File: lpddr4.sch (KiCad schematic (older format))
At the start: 43 parts, among them U1 MT53E256M16D1

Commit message: Remove note
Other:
- note removed: "TODO: connect to FPGA IO"
- note removed: "TODO\nAdd reset handling\nADD ODT/ZQ control"
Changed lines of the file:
@@
 Text GLabel 10900 2300 1    50   Input ~ 0
 VDD2
-Text Notes 7350 6050 0    98   ~ 20
-TODO\nAdd reset handling\nADD ODT/ZQ control
 Text GLabel 9350 3050 0    50   Input ~ 0
 CS0_B
@@
 Wire Wire Line
 	6175 2850 6375 2850
-Text Notes 13075 2025 0    98   ~ 20
-TODO: connect to FPGA IO
 $Comp
 L antmicroCapacitorsmisc:C_100n_0201 C1

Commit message: Add OSHW logotype
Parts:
- added N?: oshw_logo, antmicro-footprints:oshw-logo, symbol antmicroMechanicalParts:oshw_logo
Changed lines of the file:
@@
 Wire Wire Line
 	12050 3450 12050 3525
+$Comp
+L antmicroMechanicalParts:oshw_logo N?
+U 1 1 6001ECE6
+P 11900 9575
+F 0 "N?" H 12094 9578 50  0000 L CNN
+F 1 "oshw_logo" H 12094 9487 50  0000 L CNN
+F 2 "antmicro-footprints:oshw-logo" H 11920 9335 50  0001 C CNN
+F 3 "" H 11900 9575 50  0001 C CNN
+	1    11900 9575
+	1    0    0    -1
+$EndComp
 $EndSCHEMATC

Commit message: Optimize pairs of buried vias
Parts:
- gave numbers to parts that had none: 1
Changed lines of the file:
@@
 Title ""
 Date ""
-Rev ""
+Rev "1.0.0"
 Comp ""
 Comment1 ""
@@
 	12050 3450 12050 3525
 $Comp
-L antmicroMechanicalParts:oshw_logo N?
+L antmicroMechanicalParts:oshw_logo N3
 U 1 1 6001ECE6
 P 11900 9575
-F 0 "N?" H 12094 9578 50  0000 L CNN
+F 0 "N3" H 12094 9578 50  0000 L CNN
 F 1 "oshw_logo" H 12094 9487 50  0000 L CNN
 F 2 "antmicro-footprints:oshw-logo" H 11920 9335 50  0001 C CNN

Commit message: Update local libs, resolve DRC
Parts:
- C1, C10, C11, C12, C13, C14, C15, C16, C17, C18, C19, C2, C20, C21, C22, C23, C24, C25, C26, C27, C28, C29, C3, C30, C31, C32, C33, C35, C36, C4, C5, C6, C7, C8, C9: footprint antmicro-footprints:0201-res -> lpddr4-testbed-footprints:0201-res; symbol antmicroCapacitorsmisc:C_100n_0201 -> lpddr4-testbed:C_100n_0201
- N3: footprint antmicro-footprints:oshw-logo -> lpddr4-testbed-footprints:oshw-logo; symbol antmicroMechanicalParts:oshw_logo -> lpddr4-testbed:oshw_logo
- R1, R3, R4, R5: footprint antmicro-footprints:0402-res -> lpddr4-testbed-footprints:0402-res; symbol antmicroResistors0402:R_10k_0402 -> lpddr4-testbed:R_10k_0402
- R2, R7: footprint antmicro-footprints:0402-res -> lpddr4-testbed-footprints:0402-res; symbol antmicroResistors0402:R_0R_0402 -> lpddr4-testbed:R_0R_0402
- R6: footprint antmicro-footprints:0402-res -> lpddr4-testbed-footprints:0402-res; symbol antmicroResistors0402:R_240R_0402 -> lpddr4-testbed:R_240R_0402

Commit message: Update DRAM MPN
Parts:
- U1: value MT53E256M16D1 -> MT53E256M32D2DS-053; symbol lpddr4-testbed:MT53E256M16D1 -> lpddr4-testbed:MT53E256M32D2DS-053; MPN (none) -> MT53E256M32D2DS-053 WT:B; Manufacturer (none) -> Micron
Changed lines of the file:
@@
 LPDDR4
 $Comp
-L lpddr4-testbed:MT53E256M16D1 U1
+L lpddr4-testbed:MT53E256M32D2DS-053 U1
 U 1 1 602BB4A5
 P 4650 4050
-F 0 "U1" H 4125 5425 50  0000 C CNN
-F 1 "MT53E256M16D1" H 4200 2675 50  0000 C CNN
+F 0 "U1" H 4900 2675 50  0000 C CNN
+F 1 "MT53E256M32D2DS-053" H 4200 2675 50  0001 C CNN
 F 2 "lpddr4-testbed-footprints:BGA-200_10.0x14.5mm_Layout12x22_P0.80x0.65mm" H 4700 2150 50  0001 C CNN
 F 3 "" H 4550 2850 50  0001 C CNN
+F 4 "MT53E256M32D2DS-053 WT:B" H 5400 2525 50  0000 C CNN "MPN"
+F 5 "Micron" H 4950 2600 50  0000 C CNN "Manufacturer"
 	1    4650 4050
 	1    0    0    -1
@@
 	12375 2950 12375 2725
 $Comp
-L lpddr4-testbed:MT53E256M16D1 U1
+L lpddr4-testbed:MT53E256M32D2DS-053 U1
 U 2 1 602BF408
 P 10900 4050
-F 0 "U1" H 10350 5425 50  0000 C CNN
-F 1 "MT53E256M16D1" H 10450 2675 50  0000 C CNN
+F 0 "U1" H 11150 2700 50  0000 C CNN
+F 1 "MT53E256M32D2DS-053" H 10450 2675 50  0001 C CNN
 F 2 "lpddr4-testbed-footprints:BGA-200_10.0x14.5mm_Layout12x22_P0.80x0.65mm" H 10950 2150 50  0001 C CNN
 F 3 "" H 10800 2850 50  0001 C CNN
+F 4 "MT53E256M32D2DS-053 WT:B" H 11650 2550 50  0000 C CNN "MPN"
+F 5 "Micron" H 11200 2625 50  0000 C CNN "Manufacturer"
 	2    10900 4050
 	1    0    0    -1

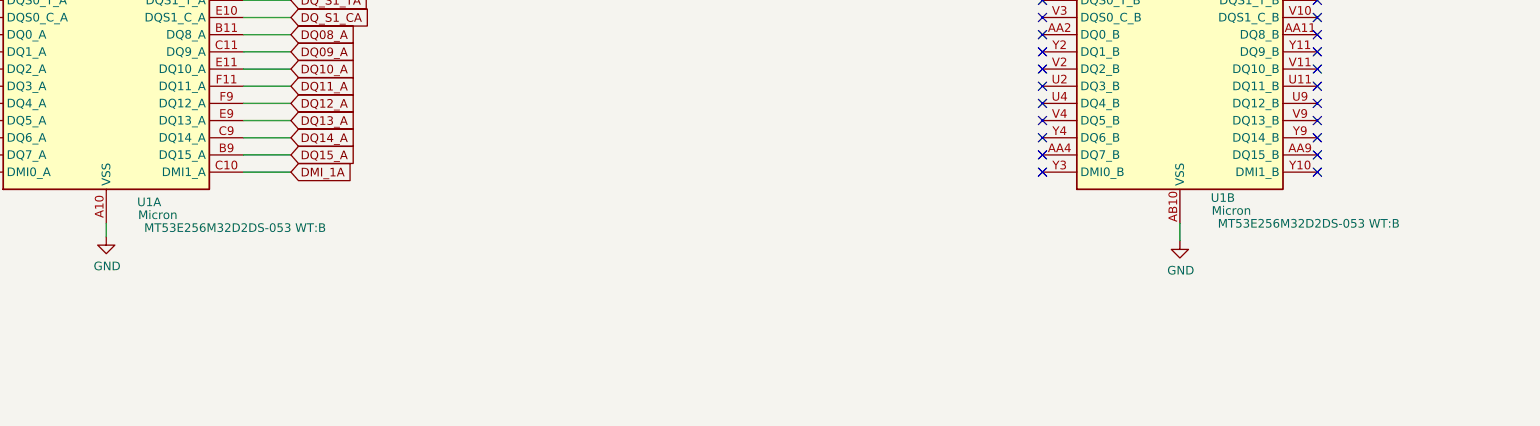
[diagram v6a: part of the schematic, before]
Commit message: Changed DDR type to MT53E1G32D2NP-046 WT:A
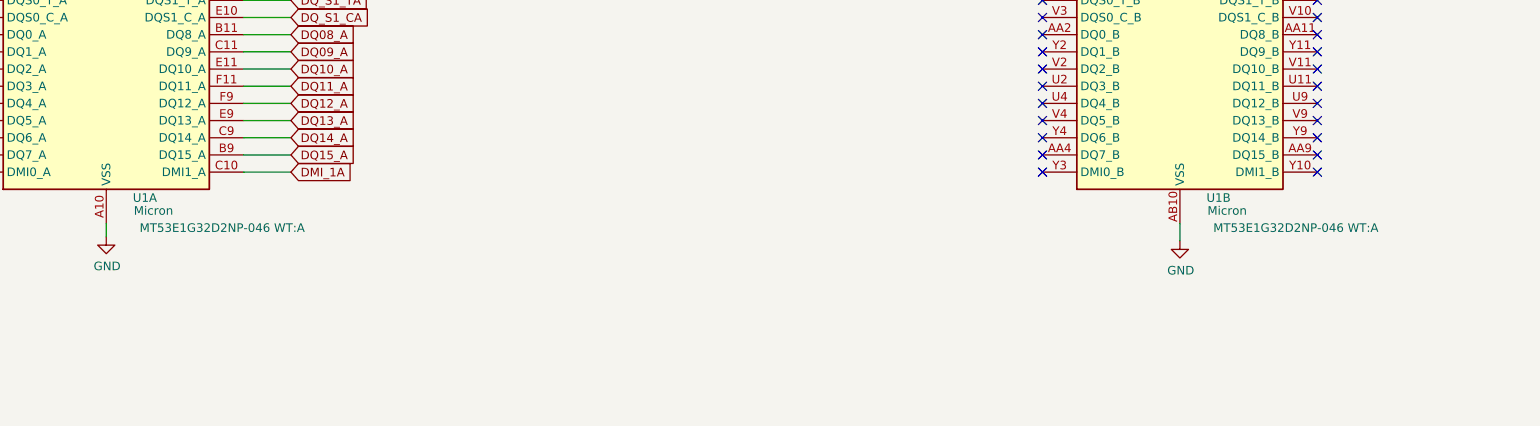
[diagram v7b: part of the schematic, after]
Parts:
- removed U1: MT53E256M32D2DS-053, lpddr4-testbed-footprints:BGA-200_10.0x14.5mm_Layout12x22_P0.80x0.65mm, symbol lpddr4-testbed:MT53E256M32D2DS-053
- added U1: MT53E1G32D2NP-046, lpddr4-testbed-footprints:BGA-200_10.0x14.5mm_Layout12x22_P0.80x0.65mm, symbol lpddr4-testbed:MT53E1G32D2NP-046
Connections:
- net CA2_A: now also U1.H9 (CA2_A)
- net CA3_A: now also U1.H10 (CA3_A)
- net CA4_A: now also U1.H11 (CA4_A)
- net CA5_A: now also U1.J11 (CA5_A)
- net CA_0A: now also U1.H2 (CA0_A)
- net CA_1A: now also U1.J2 (CA1_A)
- net CKE0_A: now also U1.J4 (CKE0_A)
- net CK_CA: now also U1.J9 (CK_C_A)
- net CK_TA: now also U1.J8 (CK_T_A)
- net CS0_A: now also U1.H4 (CS0_A)
- net CS0_B: now also U1.R4 (CS0_B)
- net DMI_0A: now also U1.C3 (DMI0_A)
- net DMI_1A: now also U1.C10 (DMI1_A)
- net DQ00_A: now also U1.B2 (DQ0_A)
- net DQ01_A: now also U1.C2 (DQ1_A)
- net DQ02_A: now also U1.E2 (DQ2_A)
- net DQ03_A: now also U1.F2 (DQ3_A)
- net DQ04_A: now also U1.F4 (DQ4_A)
- net DQ05_A: now also U1.E4 (DQ5_A)
- net DQ06_A: now also U1.C4 (DQ6_A)
- net DQ07_A: now also U1.B4 (DQ7_A)
- net DQ08_A: now also U1.B11 (DQ8_A)
- net DQ09_A: now also U1.C11 (DQ9_A)
- net DQ10_A: now also U1.E11 (DQ10_A)
- net DQ11_A: now also U1.F11 (DQ11_A)
- net DQ12_A: now also U1.F9 (DQ12_A)
- net DQ13_A: now also U1.E9 (DQ13_A)
- net DQ14_A: now also U1.C9 (DQ14_A)
- net DQ15_A: now also U1.B9 (DQ15_A)
- net DQ_S0_CA: now also U1.E3 (DQS0_C_A)
- net DQ_S0_TA: now also U1.D3 (DQS0_T_A)
- net DQ_S1_CA: now also U1.E10 (DQS1_C_A)
- net DQ_S1_TA: now also U1.D10 (DQS1_T_A)
- net GND: now also U1.A10 (VSS), U1.A3 (VSS), U1.AB10 (VSS), U1.AB3 (VSS), U1.AB5 (VSS), U1.AB8 (VSS), U1.C1 (VSS), U1.C12 (VSS), U1.C5 (VSS), U1.C8 (VSS), U1.D11 (VSS), U1.D2 (VSS), U1.D4 (VSS), U1.D9 (VSS), U1.E1 (VSS), U1.E12 (VSS), U1.E5 (VSS), U1.E8 (VSS), U1.G1 (VSS), U1.G10 (VSS), U1.G12 (VSS), U1.G3 (VSS), U1.G5 (VSS), U1.G8 (VSS), U1.J1 (VSS), U1.J10 (VSS), U1.J12 (VSS), U1.J3 (VSS), U1.K11 (VSS), U1.K2 (VSS), U1.K4 (VSS), U1.K9 (VSS), U1.N11 (VSS), U1.N2 (VSS), U1.N4 (VSS), U1.N9 (VSS), U1.P1 (VSS), U1.P10 (VSS), U1.P12 (VSS), U1.P3 (VSS), U1.T1 (VSS), U1.T10 (VSS), U1.T12 (VSS), U1.T3 (VSS), U1.T5 (VSS), U1.T8 (VSS), U1.V1 (VSS), U1.V12 (VSS), U1.V5 (VSS), U1.V8 (VSS), U1.W11 (VSS), U1.W2 (VSS), U1.W4 (VSS), U1.W9 (VSS), U1.Y1 (VSS), U1.Y12 (VSS), U1.Y5 (VSS), U1.Y8 (VSS)
- net VDD1: now also U1.F1 (VDD1), U1.F12 (VDD1), U1.G4 (VDD1), U1.G9 (VDD1), U1.T4 (VDD1), U1.T9 (VDD1), U1.U1 (VDD1), U1.U12 (VDD1)
- net VDD2: now also U1.A4 (VDD2), U1.A9 (VDD2), U1.AB4 (VDD2), U1.AB9 (VDD2), U1.F5 (VDD2), U1.F8 (VDD2), U1.H1 (VDD2), U1.H12 (VDD2), U1.H5 (VDD2), U1.H8 (VDD2), U1.K1 (VDD2), U1.K10 (VDD2), U1.K12 (VDD2), U1.K3 (VDD2), U1.N1 (VDD2), U1.N10 (VDD2), U1.N12 (VDD2), U1.N3 (VDD2), U1.R1 (VDD2), U1.R12 (VDD2), U1.R5 (VDD2), U1.R8 (VDD2), U1.U5 (VDD2), U1.U8 (VDD2)
- net VDDQ: now also U1.AA10 (VDDQ), U1.AA3 (VDDQ), U1.AA5 (VDDQ), U1.AA8 (VDDQ), U1.B10 (VDDQ), U1.B3 (VDDQ), U1.B5 (VDDQ), U1.B8 (VDDQ), U1.D1 (VDDQ), U1.D12 (VDDQ), U1.D5 (VDDQ), U1.D8 (VDDQ), U1.F10 (VDDQ), U1.F3 (VDDQ), U1.U10 (VDDQ), U1.U3 (VDDQ), U1.W1 (VDDQ), U1.W12 (VDDQ), U1.W5 (VDDQ), U1.W8 (VDDQ)
- net at R1.2, R2.1: now also U1.G2 (ODT_CA_A)
- net at R4.2: now also U1.T2 (ODT_CA_B)
- net at R5.2, R7.1: now also U1.T11 (RESET_N)
- net at R6.1: now also U1.A5 (ZQ0)
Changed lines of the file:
@@
 Text Notes 1075 1025 0    98   ~ 20
 LPDDR4
-$Comp
-L lpddr4-testbed:MT53E256M32D2DS-053 U1
-U 1 1 602BB4A5
-P 4650 4050
-F 0 "U1" H 4900 2675 50  0000 C CNN
-F 1 "MT53E256M32D2DS-053" H 4200 2675 50  0001 C CNN
-F 2 "lpddr4-testbed-footprints:BGA-200_10.0x14.5mm_Layout12x22_P0.80x0.65mm" H 4700 2150 50  0001 C CNN
-F 3 "" H 4550 2850 50  0001 C CNN
-F 4 "MT53E256M32D2DS-053 WT:B" H 5400 2525 50  0000 C CNN "MPN"
-F 5 "Micron" H 4950 2600 50  0000 C CNN "Manufacturer"
-	1    4650 4050
-	1    0    0    -1
-$EndComp
 Wire Notes Line
 	4700 11175 4675 11175
@@
 Wire Wire Line
 	12375 2950 12375 2725
-$Comp
-L lpddr4-testbed:MT53E256M32D2DS-053 U1
-U 2 1 602BF408
-P 10900 4050
-F 0 "U1" H 11150 2700 50  0000 C CNN
-F 1 "MT53E256M32D2DS-053" H 10450 2675 50  0001 C CNN
-F 2 "lpddr4-testbed-footprints:BGA-200_10.0x14.5mm_Layout12x22_P0.80x0.65mm" H 10950 2150 50  0001 C CNN
-F 3 "" H 10800 2850 50  0001 C CNN
-F 4 "MT53E256M32D2DS-053 WT:B" H 11650 2550 50  0000 C CNN "MPN"
-F 5 "Micron" H 11200 2625 50  0000 C CNN "Manufacturer"
-	2    10900 4050
-	1    0    0    -1
-$EndComp
 NoConn ~ 10100 2850
 NoConn ~ 10100 2950
@@
 	1    0    0    -1
 $EndComp
+$Comp
+L lpddr4-testbed:MT53E1G32D2NP-046 U1
+U 1 1 60819F73
+P 4650 4050
+F 0 "U1" H 4875 2700 50  0000 C CNN
+F 1 "MT53E1G32D2NP-046" H 4650 2370 50  0001 C CNN
+F 2 "lpddr4-testbed-footprints:BGA-200_10.0x14.5mm_Layout12x22_P0.80x0.65mm" H 4700 2150 50  0001 C CNN
+F 3 "" H 4550 2850 50  0001 C CNN
+F 4 "Micron" H 4925 2625 50  0000 C CNN "Manufacturer"
+F 5 "MT53E1G32D2NP-046 WT:A" H 5325 2525 50  0000 C CNN "MPN"
+	1    4650 4050
+	1    0    0    -1
+$EndComp
+$Comp
+L lpddr4-testbed:MT53E1G32D2NP-046 U1
+U 2 1 6082254C
+P 10900 4050
+F 0 "U1" H 11125 2700 50  0000 C CNN
+F 1 "MT53E1G32D2NP-046" H 10900 2370 50  0001 C CNN
+F 2 "lpddr4-testbed-footprints:BGA-200_10.0x14.5mm_Layout12x22_P0.80x0.65mm" H 10950 2150 50  0001 C CNN
+F 3 "" H 10800 2850 50  0001 C CNN
+F 4 "Micron" H 11175 2625 50  0000 C CNN "Manufacturer"
+F 5 "MT53E1G32D2NP-046 WT:A" H 11575 2525 50  0000 C CNN "MPN"
+	2    10900 4050
+	1    0    0    -1
+$EndComp
